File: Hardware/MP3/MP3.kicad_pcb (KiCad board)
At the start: 2 copper layers, 70 x 65 mm, 24 parts, among them IC1 MCP73871-2CCI_ML, IC2 TUSB320LAIRWBR, J1 Conn_02x20_Odd_Even, J2 USB_C_Receptacle_USB2.0, U1 TPS63002DRCR

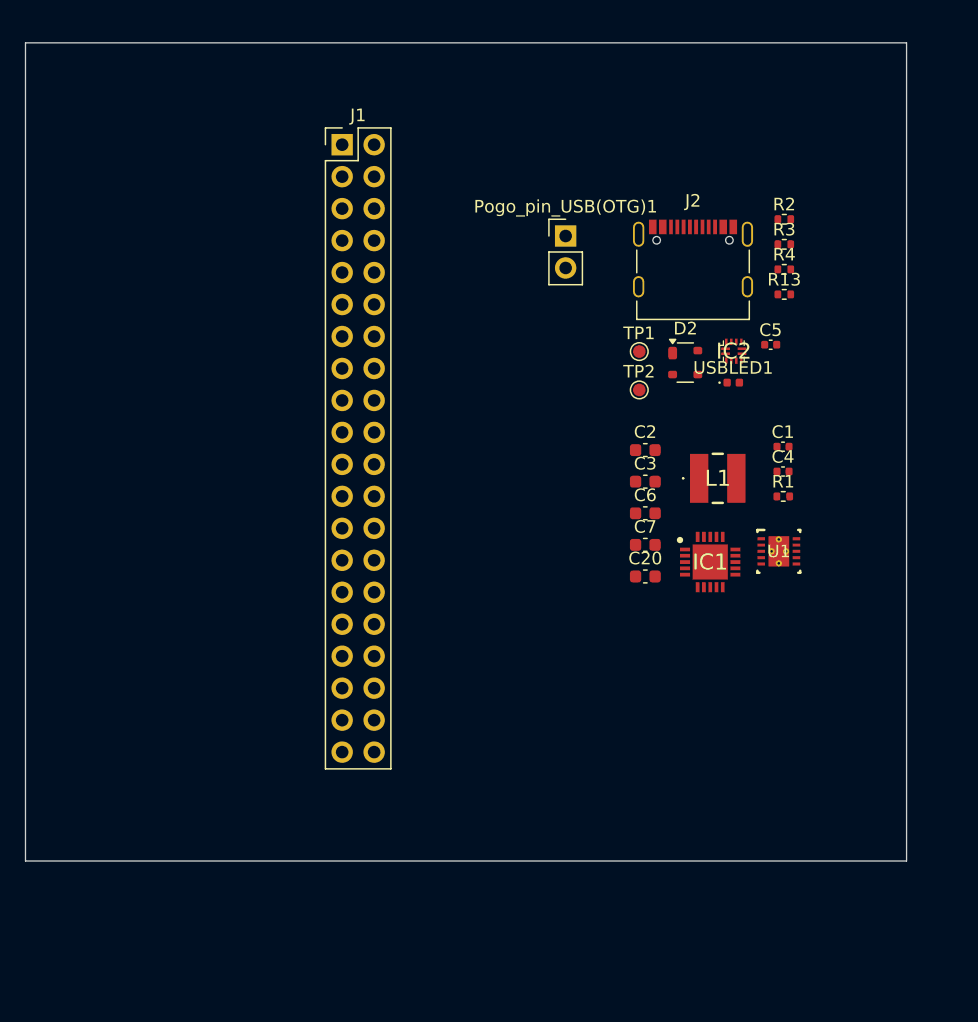
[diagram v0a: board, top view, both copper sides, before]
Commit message: Large additions, DAC schematic work started
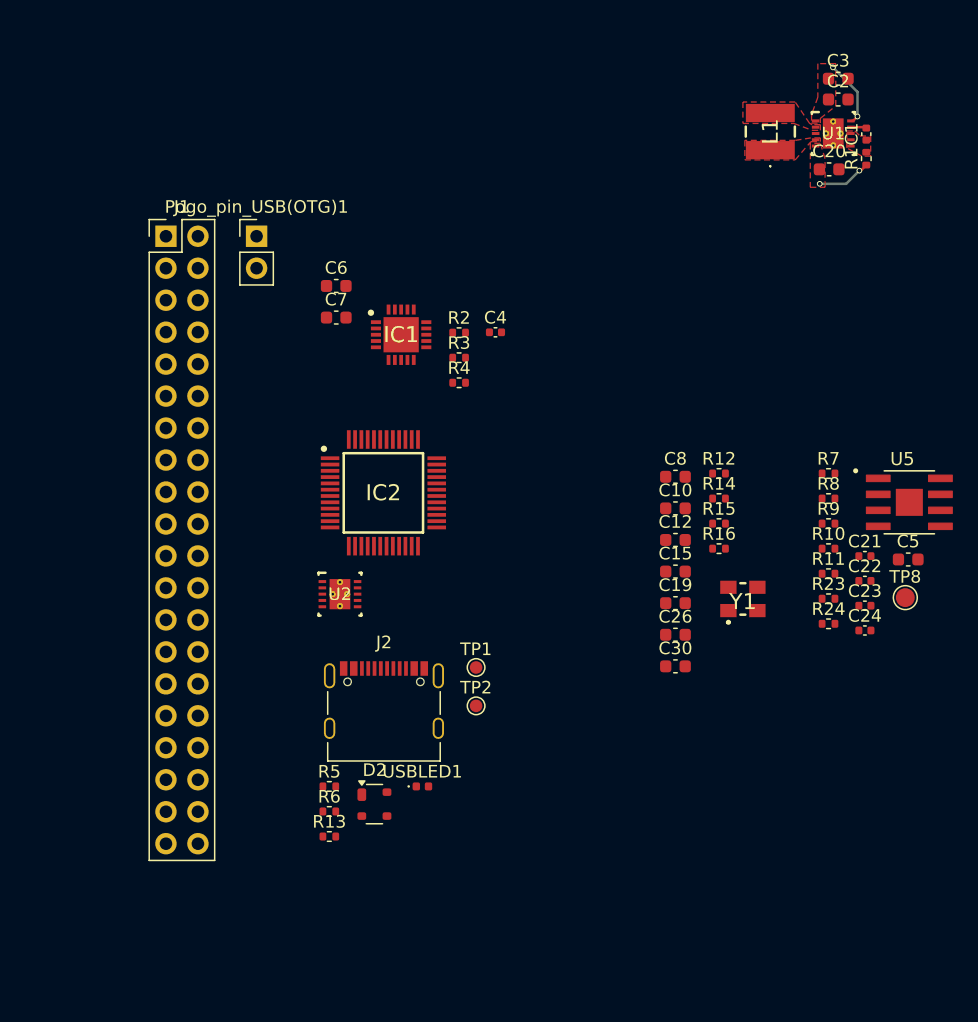
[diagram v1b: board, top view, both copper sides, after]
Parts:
- added C10: 0.1uF, Capacitor_SMD:C_0603_1608Metric, F.Cu at (126.6, 79.5)
- added C12: 0.1uF, Capacitor_SMD:C_0603_1608Metric, F.Cu at (126.6, 82.0)
- added C15: 0.1uF, Capacitor_SMD:C_0603_1608Metric, F.Cu at (126.6, 84.5)
- added C19: 0.1uF, Capacitor_SMD:C_0603_1608Metric, F.Cu at (126.6, 87.0)
- added C21: 10uF, Capacitor_SMD:C_0402_1005Metric, F.Cu at (141.7, 83.3)
- added C22: 4.7uF, Capacitor_SMD:C_0402_1005Metric, F.Cu at (141.7, 85.2)
- added C23: 10uF, Capacitor_SMD:C_0402_1005Metric, F.Cu at (141.7, 87.2)
- added C24: 0.1uF, Capacitor_SMD:C_0402_1005Metric, F.Cu at (141.7, 89.2)
- added C26: 0.1uF, Capacitor_SMD:C_0603_1608Metric, F.Cu at (126.6, 89.5)
- added C30: 0.1uF, Capacitor_SMD:C_0603_1608Metric, F.Cu at (126.6, 92.0)
- added C8: 0.1uF, Capacitor_SMD:C_0603_1608Metric, F.Cu at (126.6, 77.0)
- added R10: 100k, Resistor_SMD:R_0402_1005Metric, F.Cu at (138.8, 82.7)
- added R11: 10k, Resistor_SMD:R_0402_1005Metric, F.Cu at (138.8, 84.7)
- added R12: 10, Resistor_SMD:R_0402_1005Metric, F.Cu at (130.1, 76.7)
- added R14: 10, Resistor_SMD:R_0402_1005Metric, F.Cu at (130.1, 78.7)
- added R15: 10, Resistor_SMD:R_0402_1005Metric, F.Cu at (130.1, 80.7)
- added R16: 10, Resistor_SMD:R_0402_1005Metric, F.Cu at (130.1, 82.7)
- added R23: 56k, Resistor_SMD:R_0402_1005Metric, F.Cu at (138.8, 86.7)
- added R24: 10k, Resistor_SMD:R_0402_1005Metric, F.Cu at (138.8, 88.7)
- added R5: 5.1k, Resistor_SMD:R_0402_1005Metric, F.Cu at (99.1, 101.6)
- added R6: 5.1k, Resistor_SMD:R_0402_1005Metric, F.Cu at (99.1, 103.6)
- added R7: 10k, Resistor_SMD:R_0402_1005Metric, F.Cu at (138.8, 76.7)
- added R8: 10k, Resistor_SMD:R_0402_1005Metric, F.Cu at (138.8, 78.7)
- added R9: 330k, Resistor_SMD:R_0402_1005Metric, F.Cu at (138.8, 80.7)
- added TP8: TestPoint, TestPoint:TestPoint_Pad_D1.5mm, F.Cu at (144.9, 86.6)
- added U2: OPA1622IDRCR, iclr:DRC0010J, F.Cu at (100.0, 86.3)
- added U5: SC4215, iclr:SOIC127P599X175-9N, F.Cu at (145.2, 79.0)
- added Y1: ABM8-22.5792MHZ-D2Y-T, iclr:ABM810000MHZ12D2W, F.Cu at (132.0, 86.7)
- C5: value 0.1uF -> 10uF; footprint Capacitor_SMD:C_0402_1005Metric -> Capacitor_SMD:C_0603_1608Metric
- IC2: value TUSB320LAIRWBR -> AK4493SEQ; footprint iclr:RWB0012A -> iclr:QFP50P900X900X160-48N
- R2: value 10k -> 2.49k
- R3: value 10k -> 24.9k
- R4: value 900k -> 2.0k
- moved R13 56.2 mm to (99.1, 105.6)
- moved D2 42.9 mm to (102.7, 103.0)
- moved J2 42.8 mm to (103.5, 94.7)
- moved USBLED1 40.5 mm to (106.5, 101.6)
- moved C3 35.5 mm to (139.6, 45.4)
- moved C20 35.5 mm to (138.8, 52.5)
- moved U1 33.5 mm to (139.2, 49.7)
- moved C2 31.8 mm to (139.6, 47.0)
- moved IC1 30.5 mm to (104.8, 65.7)
- moved C6 30.5 mm to (99.7, 61.8)
- moved C7 30.5 mm to (99.7, 64.3)
- moved IC2 30.0 mm to (103.4, 78.2)
- moved TP1 28.3 mm to (110.8, 92.1)
- moved TP2 28.3 mm to (110.8, 95.2)
- moved L1 27.9 mm to (134.2, 49.6), turned to 90 degrees
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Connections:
- net /Power/Vout renamed /Power/MCPout
- net /USB-C/Audio_detected renamed /DAC+AMP/WCK
- net /USB-C/DFP renamed /DAC+AMP/SDA
- net /USB-C/OUT1 renamed /DAC+AMP/CS
- net /USB-C/OUT2 renamed /DAC+AMP/SCL
- C5 pad 1: 5V -> VBUS
- IC1 pad 12: unconnected-(IC1-PROG3-Pad12) -> Net-(IC1-PROG3)
- IC1 pad 13: unconnected-(IC1-PROG1-Pad13) -> Net-(IC1-PROG1)
- IC1 pad 17: unconnected-(IC1-CE-Pad17) -> /Power/CE
- IC1 pad 2: VBUS -> Net-(IC1-VPCC)
- IC1 pad 3: unconnected-(IC1-SEL-Pad3) -> GND
- IC1 pad 4: unconnected-(IC1-PROG2-Pad4) -> 3V3
- IC1 pad 5: unconnected-(IC1-THERM-Pad5) -> Net-(IC1-THERM)
- IC1 pad 6: unconnected-(IC1-~{PG}-Pad6) -> /Power/PG
- IC1 pad 7: unconnected-(IC1-STAT2-Pad7) -> /Power/STAT2
- IC1 pad 8: unconnected-(IC1-STAT1/~{LBO}-Pad8) -> /Power/LBO
- IC1 pad 9: unconnected-(IC1-~{TE}-Pad9) -> GND
- IC2 pad 1: /USB-C/CC1 -> Net-(IC2-DVDD)
- IC2 pad 10: GND -> unconnected-(IC2-DIF0/DZFL-Pad10)
- IC2 pad 11: Net-(IC2-EN) -> unconnected-(IC2-DIF1/DZFR-Pad11)
- IC2 pad 12: 5V -> unconnected-(IC2-DIF2/CAD0-Pad12)
- IC2 pad 2: /USB-C/CC2 -> /DAC+AMP/PDN
- IC2 pad 3: Net-(IC2-PORT) -> /DAC+AMP/BICK
- IC2 pad 4: Net-(IC2-VBUS_DET) -> /DAC+AMP/SDATA
- IC2 pad 5: unconnected-(IC2-ADDR-Pad5) -> /DAC+AMP/LRCK
- J2 pad A5: /USB-C/CC1 -> Net-(J2-CC1)
- J2 pad B5: /USB-C/CC2 -> Net-(J2-CC2)
- R2 pad 1: Net-(IC2-PORT) -> GND
- R2 pad 2: GND -> Net-(IC1-PROG1)
- R3 pad 1: Net-(IC2-EN) -> GND
- R3 pad 2: GND -> Net-(IC1-PROG3)
- R4 pad 1: Net-(IC2-VBUS_DET) -> unconnected-(R4-Pad1)
- R4 pad 2: VBUS -> GND
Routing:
- net 5V: track 0.00 -> 5.38 mm, vias 0 -> 2
- net /Power/MCPout: track 0.00 -> 4.32 mm, vias 0 -> 2
- net GND: track 0.00 -> 1.25 mm
- added copper zone on F.Cu, net /Power/MCPout
- added copper zone on F.Cu, net 5V
- added copper zone on F.Cu, net Net-(U1-EN)
- added copper zone on F.Cu, net Net-(U1-L1)
- added copper zone on F.Cu, net Net-(U1-L2)
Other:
- board outline removed
- copper layers 2 -> 4

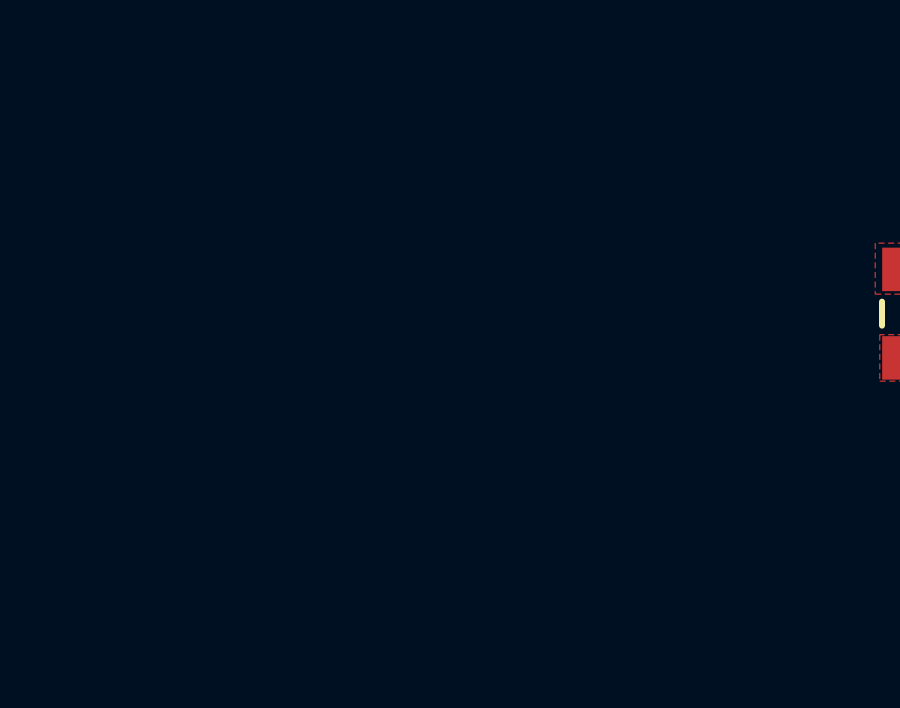
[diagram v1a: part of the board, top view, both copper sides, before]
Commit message: feat: Made some changes to the DAC. Explicitly using register control (using I2C) with PCM audio. Planning to use 5.2V buck on 5V line, then Low noise LDO VREF for DAC, another for AMP power, and a 3v3 low noise LDO for DAC too.
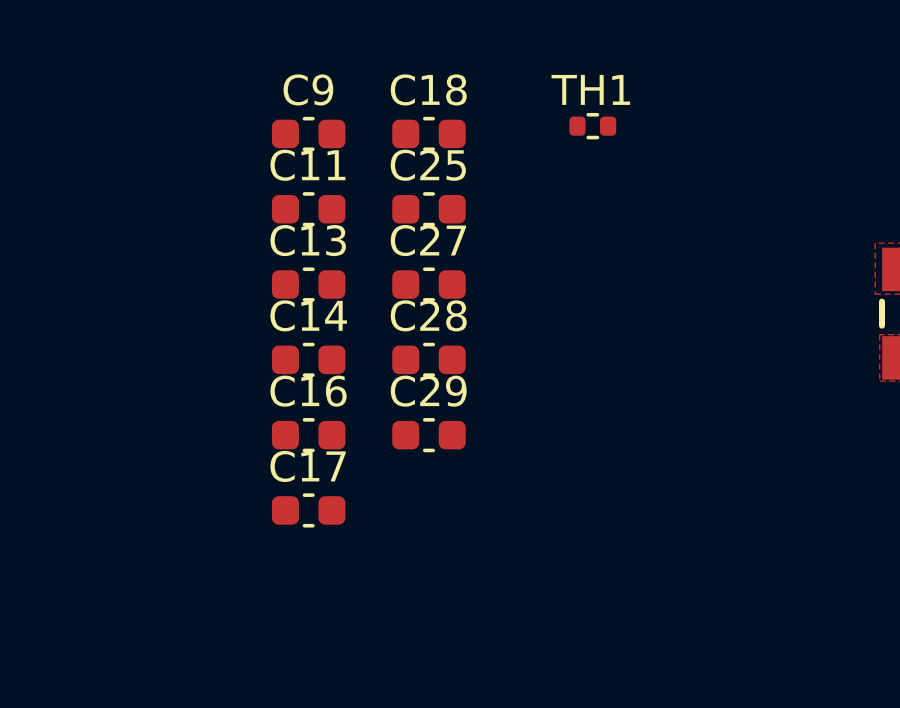
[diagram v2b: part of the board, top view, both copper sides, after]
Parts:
- added C11: 10uF, Capacitor_SMD:C_0603_1608Metric, F.Cu at (113.1, 46.1)
- added C13: 10uF, Capacitor_SMD:C_0603_1608Metric, F.Cu at (113.1, 48.6)
- added C14: 10uF, Capacitor_SMD:C_0603_1608Metric, F.Cu at (113.1, 51.1)
- added C16: 470uF, Capacitor_SMD:C_0603_1608Metric, F.Cu at (113.1, 53.6)
- added C17: 10uF, Capacitor_SMD:C_0603_1608Metric, F.Cu at (113.1, 56.1)
- added C18: 10uF, Capacitor_SMD:C_0603_1608Metric, F.Cu at (117.1, 43.6)
- added C25: 10uF, Capacitor_SMD:C_0603_1608Metric, F.Cu at (117.1, 46.1)
- added C27: 470uF, Capacitor_SMD:C_0603_1608Metric, F.Cu at (117.1, 48.6)
- added C28: 10uF, Capacitor_SMD:C_0603_1608Metric, F.Cu at (117.1, 51.1)
- added C29: 10uF, Capacitor_SMD:C_0603_1608Metric, F.Cu at (117.1, 53.6)
- added C9: 10uF, Capacitor_SMD:C_0603_1608Metric, F.Cu at (113.1, 43.6)
- added TH1: Thermistor_NTC 10k, Resistor_SMD:R_0402_1005Metric, F.Cu at (122.6, 43.3)
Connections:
- IC2 pad 12: unconnected-(IC2-DIF2/CAD0-Pad12) -> GND
- IC2 pad 14: unconnected-(IC2-I2C/INV-Pad14) -> /DAC+AMP/I2C
- IC2 pad 15: unconnected-(IC2-DEM0-Pad15) -> GND
- IC2 pad 17: unconnected-(IC2-ACKS/CAD1-Pad17) -> GND
- IC2 pad 46: unconnected-(IC2-MCLK-Pad46) -> /DAC+AMP/CLOCK
- IC2 pad 6: /DAC+AMP/WCK -> GND
- IC2 pad 7: /DAC+AMP/CS -> GND

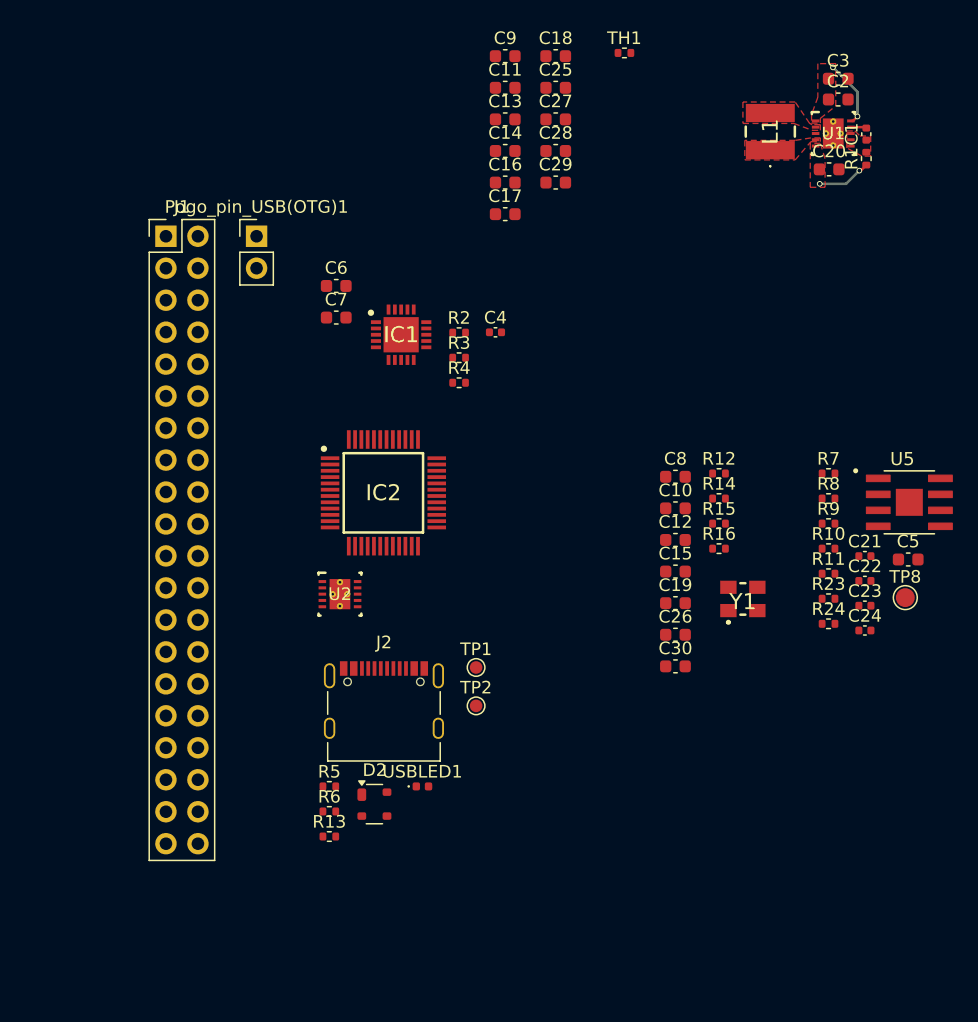
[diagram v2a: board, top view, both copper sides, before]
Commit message: feat: Large progress made on the power system. Next steps, find oscillator, sort out LDO footprints, add OLED connectors and encoder connector.
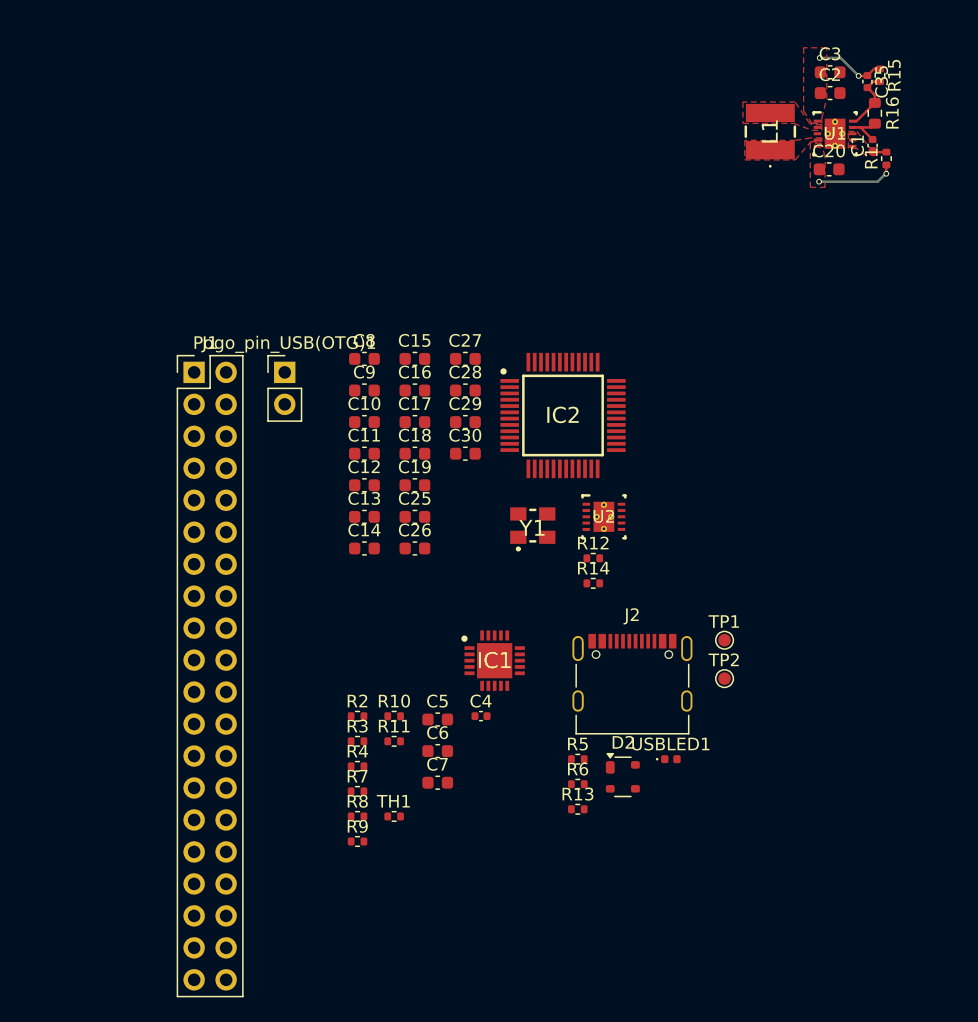
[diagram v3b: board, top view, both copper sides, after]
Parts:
- removed C21, C23: 10uF, Capacitor_SMD:C_0402_1005Metric
- removed C22: 4.7uF, Capacitor_SMD:C_0402_1005Metric
- removed C24: 0.1uF, Capacitor_SMD:C_0402_1005Metric
- removed R23: 56k, Resistor_SMD:R_0402_1005Metric
- removed R24: 10k, Resistor_SMD:R_0402_1005Metric
- removed TP8: TestPoint, TestPoint:TestPoint_Pad_D1.5mm
- removed U5: SC4215, iclr:SOIC127P599X175-9N
- added C35: 1nF, Capacitor_SMD:C_0402_1005Metric, F.Cu at (141.9, 45.6)
- C2: value 10uF -> 22uF
- C3: value 10uF -> 47uF
- R15: value 10 -> 1.96MΩ
- R16: value 10 -> 208kΩ; footprint Resistor_SMD:R_0402_1005Metric -> Resistor_SMD:R_0603_1608Metric
- U1: value TPS63002DRCR -> TPS63000DRCR
- moved TH1 63.4 mm to (104.3, 104.0)
- moved R9 45.1 mm to (101.4, 106.0)
- moved R7 45.1 mm to (101.4, 102.0)
- moved R8 45.1 mm to (101.4, 104.0)
- moved C5 39.5 mm to (107.8, 96.3)
- moved R15 37.8 mm to (142.9, 45.1), turned to -90 degrees
- moved C6 37.8 mm to (107.8, 98.8)
- moved C7 37.8 mm to (107.8, 101.3)
- moved R10 37.0 mm to (104.3, 96.0)
- moved R11 37.0 mm to (104.3, 98.0)
- moved R16 36.7 mm to (142.5, 48.1), turned to -90 degrees
- moved C25 35.9 mm to (105.9, 80.2)
- moved C13 33.5 mm to (101.9, 80.2)
- moved C14 33.5 mm to (101.9, 82.7)
- moved C18 33.5 mm to (105.9, 75.1)
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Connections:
- C16 pad 1: 5V -> +A5V
- C18 pad 1: /DAC+AMP/VDL -> +A5V
- C19 pad 1: /DAC+AMP/VDL -> +A5V
- C2 pad 1: 5V -> +5.2V
- C25 pad 1: /DAC+AMP/VDR -> +A5V
- C26 pad 1: /DAC+AMP/VDR -> +A5V
- C27 pad 1: 5V -> +A5V
- C3 pad 1: 5V -> +5.2V
- IC2 pad 25: unconnected-(IC2-AOUTRP-Pad25) -> /DAC+AMP/RIGHT+
- IC2 pad 26: unconnected-(IC2-AOUTRN-Pad26) -> /DAC+AMP/RIGHT-
- IC2 pad 27: /DAC+AMP/VDR -> +A5V
- IC2 pad 28: /DAC+AMP/VDR -> +A5V
- IC2 pad 33: /DAC+AMP/VDL -> +A5V
- IC2 pad 34: /DAC+AMP/VDL -> +A5V
- IC2 pad 35: unconnected-(IC2-AOUTLN-Pad35) -> /DAC+AMP/LEFT-
- IC2 pad 36: unconnected-(IC2-AOUTLP-Pad36) -> /DAC+AMP/LEFT+
- R12 pad 1: 5V -> +A5V
- R14 pad 1: 5V -> +A5V
- R15 pad 1: 5V -> +5.2V
- R15 pad 2: /DAC+AMP/VDL -> /Power/FB
- R16 pad 1: 5V -> /Power/FB
- R16 pad 2: /DAC+AMP/VDR -> GND
- U1 pad 1: 5V -> +5.2V
- U1 pad 10: 5V -> /Power/FB
- U2 pad 1: unconnected-(U2-INA+-Pad1) -> /DAC+AMP/LEFT+
- U2 pad 10: unconnected-(U2-INA--Pad10) -> /DAC+AMP/LEFT-
- U2 pad 11: unconnected-(U2-PAD-Pad11) -> GND
- U2 pad 2: unconnected-(U2-V+-Pad2) -> +5V
- U2 pad 3: unconnected-(U2-GND-Pad3) -> GND
- U2 pad 4: unconnected-(U2-V--Pad4) -> GND
- U2 pad 5: unconnected-(U2-INB+-Pad5) -> /DAC+AMP/RIGHT+
- U2 pad 6: unconnected-(U2-INB--Pad6) -> /DAC+AMP/RIGHT-
- U2 pad 7: unconnected-(U2-OUTB-Pad7) -> /DAC+AMP/RIGHT
- U2 pad 9: unconnected-(U2-OUTA-Pad9) -> /DAC+AMP/LEFT
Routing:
- net +5.2V: track 0.00 -> 5.61 mm, vias 0 -> 2
- net 5V: track 5.38 -> 0.00 mm, vias 2 -> 0
- net /Power/FB: track 0.00 -> 5.01 mm
- net /Power/MCPout: track 4.32 -> 6.31 mm
- net GND: track 1.25 -> 3.24 mm
- net Net-(U1-EN): track 0.00 -> 1.12 mm
- added copper zone on F.Cu, net +5.2V
- removed copper zone on F.Cu, net 5V
